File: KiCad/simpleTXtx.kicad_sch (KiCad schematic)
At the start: 13 parts, among them J1 BAT, J2 VIDEO, Q1 2SC1815

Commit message: update project
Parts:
- removed J1: BAT, Connector_PinHeader_2.54mm:PinHeader_1x02_P2.54mm_Vertical, symbol Connector:Conn_01x02_Female
- removed J2: VIDEO, Connector_PinHeader_2.54mm:PinHeader_1x02_P2.54mm_Vertical, symbol Connector:Conn_01x02_Female
- added J2: power, Connector_BarrelJack:BarrelJack_GCT_DCJ200-10-A_Horizontal, symbol Connector:Barrel_Jack_MountingPin
- added J3: RCJ-044, RCJ-044:CUI_RCJ-044, symbol RCJ-044:RCJ-044
- C3, C4: footprint Capacitor_THT:C_Disc_D4.3mm_W1.9mm_P5.00mm -> Capacitor_THT:C_Disc_D11.0mm_W5.0mm_P5.00mm
- RV1: footprint Potentiometer_THT:Potentiometer_Bourns_3266Y_Vertical -> Potentiometer_THT:Potentiometer_Runtron_RM-065_Vertical
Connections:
- net GND: now also J2.2, J2.MP (MountPin), J3.1
- net at C5.2: now also J3.2
- net at C1.2, L1.1, R2.2: now also J2.1

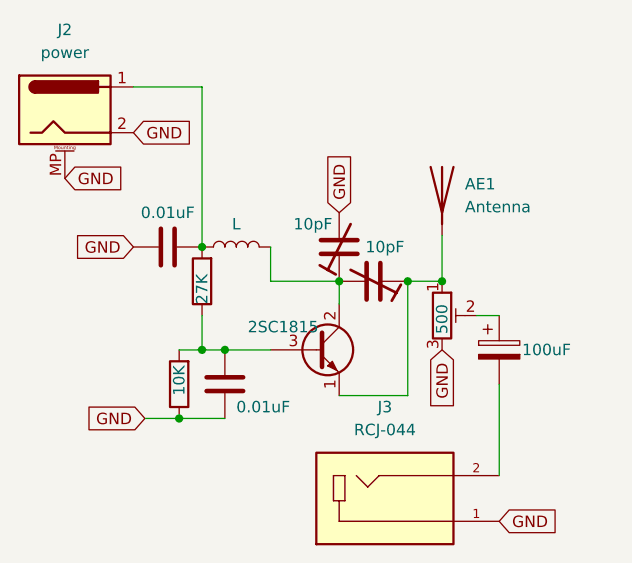
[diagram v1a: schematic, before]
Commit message: remove one trimmer
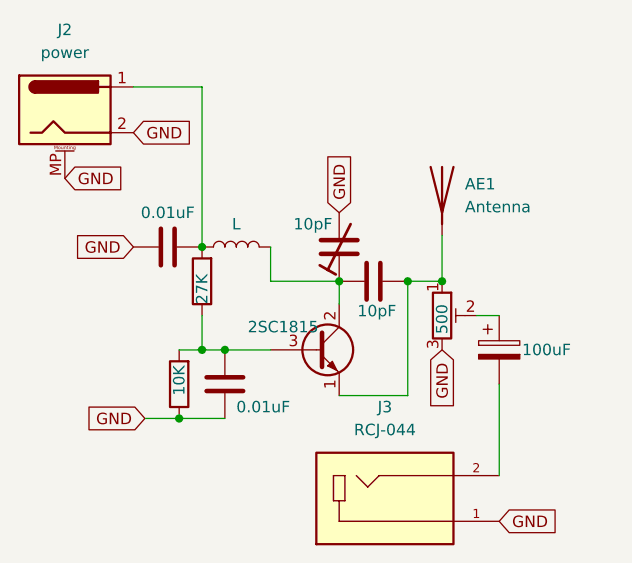
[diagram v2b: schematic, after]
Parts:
- removed C4: 10pF, Capacitor_THT:C_Disc_D11.0mm_W5.0mm_P5.00mm, symbol Device:C_Trim
- added C6: 10pF, Capacitor_THT:C_Disc_D4.3mm_W1.9mm_P5.00mm, symbol Device:C
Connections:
- net at C3.1, L1.2, Q1.2 (C): now also C6.2
- net at AE1.1 (A), Q1.1 (E), RV1.1: now also C6.1
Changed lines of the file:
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@@
+	)
+	(symbol
+		(lib_id "Device:C")
+		(at 138.43 66.04 270)
+		(unit 1)
+		(exclude_from_sim no)
+		(in_bom yes)
+		(on_board yes)
+		(dnp no)
+		(property "Reference" "C6"
+			(at 135.89 64.77 0)
+			(effects
+				(font
+					(size 1.27 1.27)
+				)
+				(justify right)
+				(hide yes)
+			)
+		)
+		(property "Value" "10pF"
+			(at 140.97 69.342 90)
+			(effects
+				(font
+					(size 1.27 1.27)
+				)
+				(justify right)
+			)
+		)
+		(property "Footprint" "Capacitor_THT:C_Disc_D4.3mm_W1.9mm_P5.00mm"
+			(at 134.62 67.0052 0)
+			(effects
+				(font
+					(size 1.27 1.27)
+				)
+				(hide yes)
+			)
+		)
+		(property "Datasheet" "~"
+			(at 138.43 66.04 0)
+			(effects
+				(font
+					(size 1.27 1.27)
+				)
+				(hide yes)
+			)
+		)
+		(property "Description" ""
+			(at 138.43 66.04 0)
+			(effects
+				(font
+					(size 1.27 1.27)
+				)
+				(hide yes)
+			)
+		)
+		(pin "1"
+		)
+		(pin "2"
+		)
+		(instances
+			(project "simpleTXtx"
+				(path "/fbc081e3-fe18-474e-9d10-ef8b1f62625c"
+					(reference "C6")
+					(unit 1)
+				)
+			)
+		)
 	)
 	(symbol
@@
 					(unit 1)
 				)
-			)
-		)
-	)
-	(symbol
-		(lib_id "Device:C_Trim")
-		(at 138.43 66.04 270)
-		(unit 1)
-		(exclude_from_sim no)
-		(in_bom yes)
-		(on_board yes)
-		(dnp no)
-		(property "Reference" "C4"
-			(at 138.43 63.5 90)
-			(effects
-				(font
-					(size 1.27 1.27)
-				)
-				(hide yes)
-			)
-		)
-		(property "Value" "10pF"
-			(at 139.7 62.23 90)
-			(effects
-				(font
-					(size 1.27 1.27)
-				)
-			)
-		)
-		(property "Footprint" "Capacitor_THT:C_Disc_D11.0mm_W5.0mm_P5.00mm"
-			(at 138.43 66.04 0)
-			(effects
-				(font
-					(size 1.27 1.27)
-				)
-				(hide yes)
-			)
-		)
-		(property "Datasheet" "~"
-			(at 138.43 66.04 0)
-			(effects
-				(font
-					(size 1.27 1.27)
-				)
-				(hide yes)
-			)
-		)
-		(property "Description" ""
-			(at 138.43 66.04 0)
-			(effects
-				(font
-					(size 1.27 1.27)
-				)
-				(hide yes)
-			)
-		)
-		(pin "1"
-		)
-		(pin "2"
-		)
-		(instances
-			(project ""
-				(path "/fbc081e3-fe18-474e-9d10-ef8b1f62625c"
-					(reference "C4")
-					(unit 1)
-				)
